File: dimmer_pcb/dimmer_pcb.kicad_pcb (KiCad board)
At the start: 2 copper layers, 99.5 x 74 mm, 35 parts, among them J1 LAMP, J2 MAINS, J4 Switch, K1 G5RLE-1, Q1 IRF740, Q2 BC847, U1 4N35, U2 WeMos_D1_mini

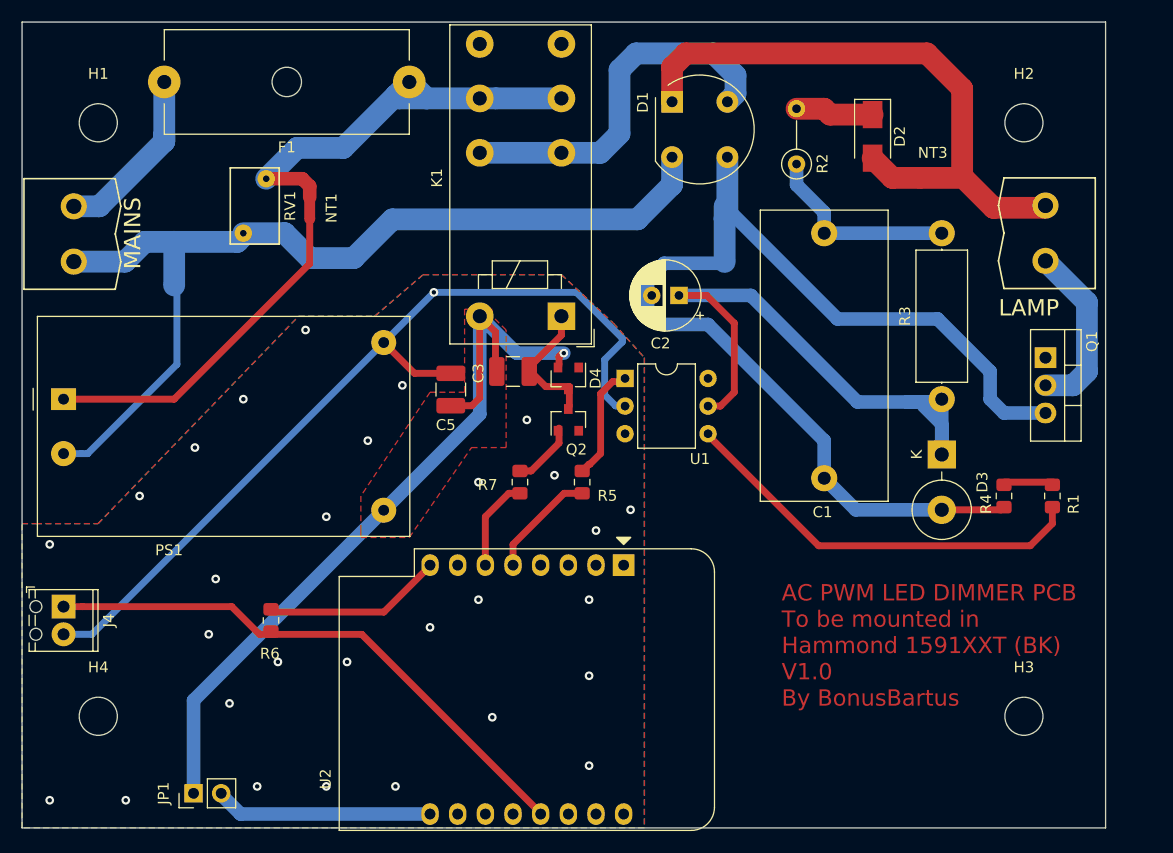
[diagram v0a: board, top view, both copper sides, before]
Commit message: updated pcb, moved text to silkscreen cleaned up silkscreen moved traced to have a nicer layout switched rectifier bridge
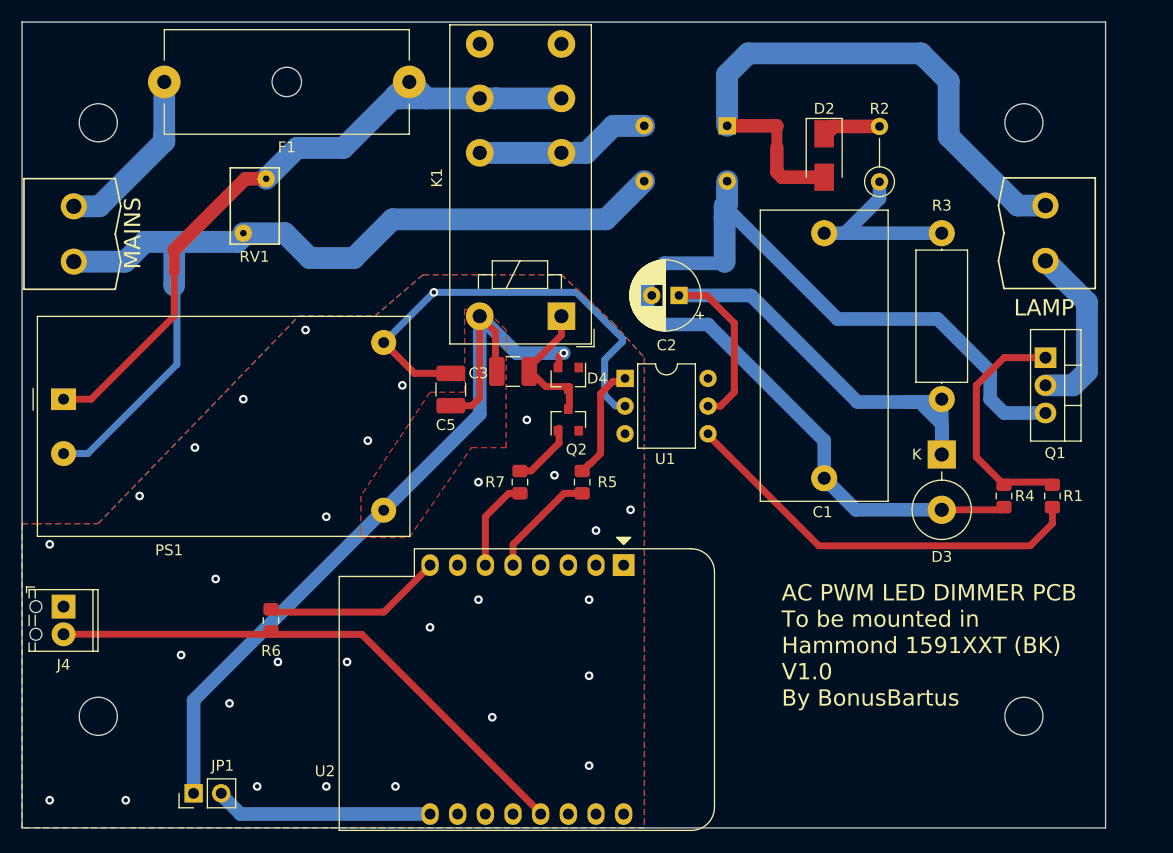
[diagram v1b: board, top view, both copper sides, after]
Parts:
- D1: value W06G -> DF10M; footprint Diode_THT:Diode_Bridge_Round_D9.8mm -> Diode_THT:Diode_Bridge_DIP-4_W7.62mm_P5.08mm; moved to B.Cu
- NT3: footprint NetTie:NetTie-2_SMD_Pad2.0mm -> NetTie:NetTie-2_SMD_Pad1.0mm
- U1: value 4N35 -> 4N35 (M by ON Semi )
- moved NT3 15.6 mm to (159.3, 86.6), turned to 270 degrees
- moved NT1 13.4 mm to (104.0, 97.9)
- moved R2 7.79 mm to (168.7, 90.7)
- moved D1 5.52 mm to (154.8, 85.5), turned to 180 degrees
- moved D2 4.78 mm to (163.7, 88.3)
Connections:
- net Net-(R6-Pad1) renamed +3V3
- D1 pad 2: MAINS-AC-HP-N -> MAINS-DC-HP_-
- D1 pad 3: MAINS-DC-HP_- -> MAINS-AC-HP-N
- J4 pad 1: Net-(J4-Pad1) -> GND
- J4 pad 2: GND -> Net-(J4-Pad2)
- R6 pad 2: Net-(J4-Pad1) -> Net-(J4-Pad2)
- U2 pad 13: Net-(J4-Pad1) -> Net-(J4-Pad2)
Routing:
- net Net-(J4-Pad1): track 51.7 -> 0.00 mm
- net Net-(J4-Pad2): track 0.00 -> 50.6 mm
- net GND: track 81.7 -> 41.2 mm
- net MAINS-AC-HP-L-FROM-RELAY: track 34.3 -> 16.1 mm
- net Net-(Q1-Pad1): track 4.57 -> 22.2 mm
- net MAINS-AC-LP-L: track 31.9 -> 17.4 mm
- net MAINS-AC-HP-L: track 41.7 -> 47.6 mm
- net MAINS-AC-HP-N: track 62.2 -> 57.2 mm
- net MAINS-DC-HP_-: track 45.8 -> 42.8 mm
- net Net-(D2-Pad1): track 7.56 -> 5.36 mm
- net MAINS-DC-LP_+: track 5.10 -> 6.77 mm
- net Net-(C1-Pad1): track 18.2 -> 16.8 mm
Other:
- net class HV-HP: clearance 0.6 -> 0.4
- net class HV-LP: clearance 0.6 -> 0.4
